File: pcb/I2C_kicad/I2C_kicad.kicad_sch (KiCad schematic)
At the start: 0 parts

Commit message: Reorganized file layout; created umbrella I2C folder for Kicad
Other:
- company: RoboCup -> (none)
- title: IMU -> (none)
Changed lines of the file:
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@@
 	(generator_version "10.0")
 	(paper "A4")
-	(title_block
-		(title "IMU")
-		(company "RoboCup")
-		(comment 1 "RoboCup DoubleKrish")
-	)
 	(sheet_instances
 		(path "/"

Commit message: added subsheets to the I2C file
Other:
- added sheet Color Sensor (ColorSensor.kicad_sch)
- added sheet GPIO expander (GPIOexpander.kicad_sch)
- added sheet Hall Effect Sensor (HallEffect.kicad_sch)
- added sheet IMU (IMU.kicad_sch)
- added sheet LED PWM Controller (LEDPWMController.kicad_sch)
- added sheet Temperature Sensor (TemperatureSensor.kicad_sch)
- company: (none) -> RoboCup
- title: (none) -> All 6 I2C Devices

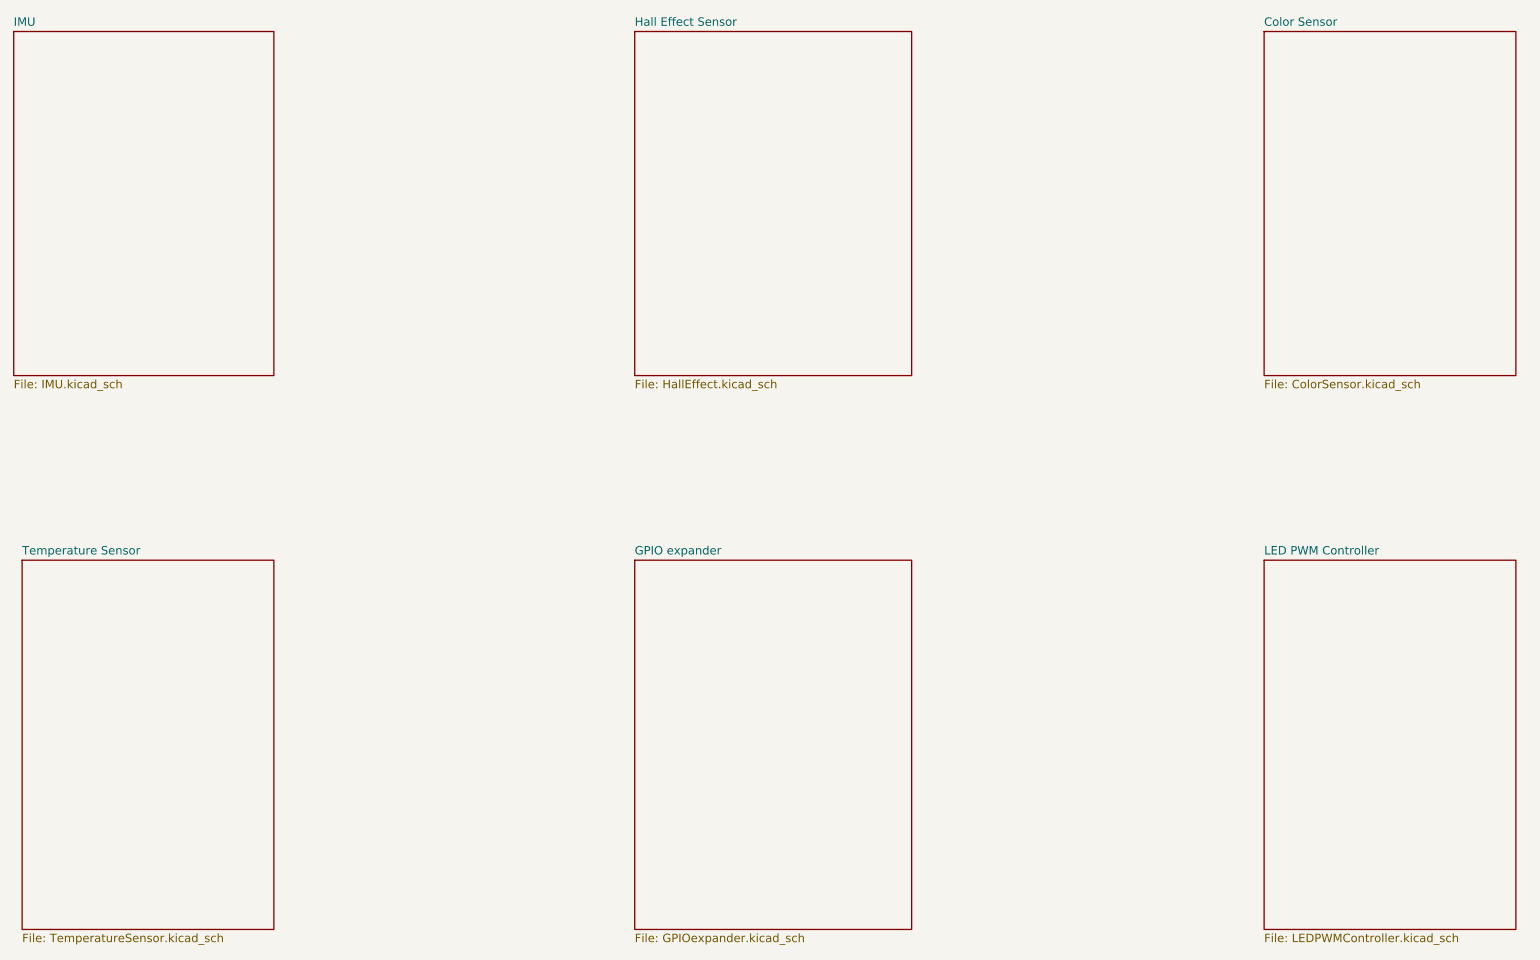
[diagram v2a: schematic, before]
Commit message: I worked on the color sensor and also the gpio expander. I added the pull ups for the SDA and SCL on the color sensor so no need to add any more. Just put do not populate for the other I2c devices
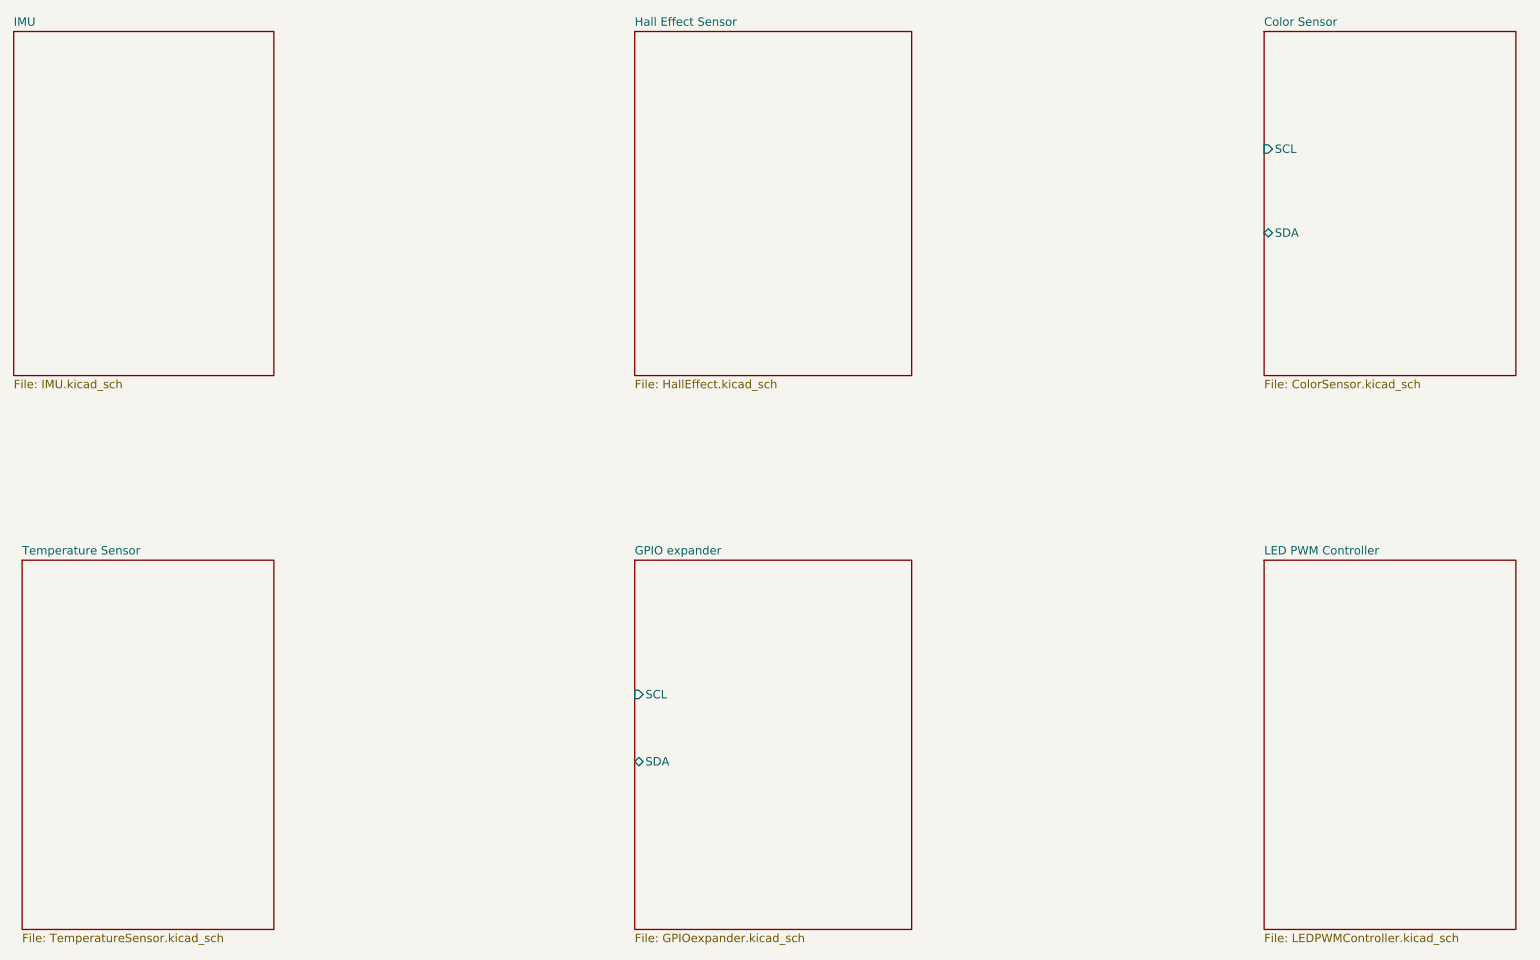
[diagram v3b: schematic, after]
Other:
- sheet Color Sensor ports: added SCL, SDA; removed none
- sheet GPIO expander ports: added SCL, SDA; removed none
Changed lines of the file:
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@@
+			)
+		)
+		(pin "SCL" input
+			(at 113.03 120.65 180)
+			(effects
+				(font
+					(size 1.27 1.27)
+				)
+				(justify left)
+			)
+		)
+		(pin "SDA" bidirectional
+			(at 113.03 130.81 180)
+			(effects
+				(font
+					(size 1.27 1.27)
+				)
+				(justify left)
 			)
 		)
@@
 			)
 		)
+		(pin "SCL" input
+			(at 208.28 38.1 180)
+			(effects
+				(font
+					(size 1.27 1.27)
+				)
+				(justify left)
+			)
+		)
+		(pin "SDA" bidirectional
+			(at 208.28 50.8 180)
+			(effects
+				(font
+					(size 1.27 1.27)
+				)
+				(justify left)
+			)
+		)

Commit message: Add IMU, Hall effect, and temp sensor sheets
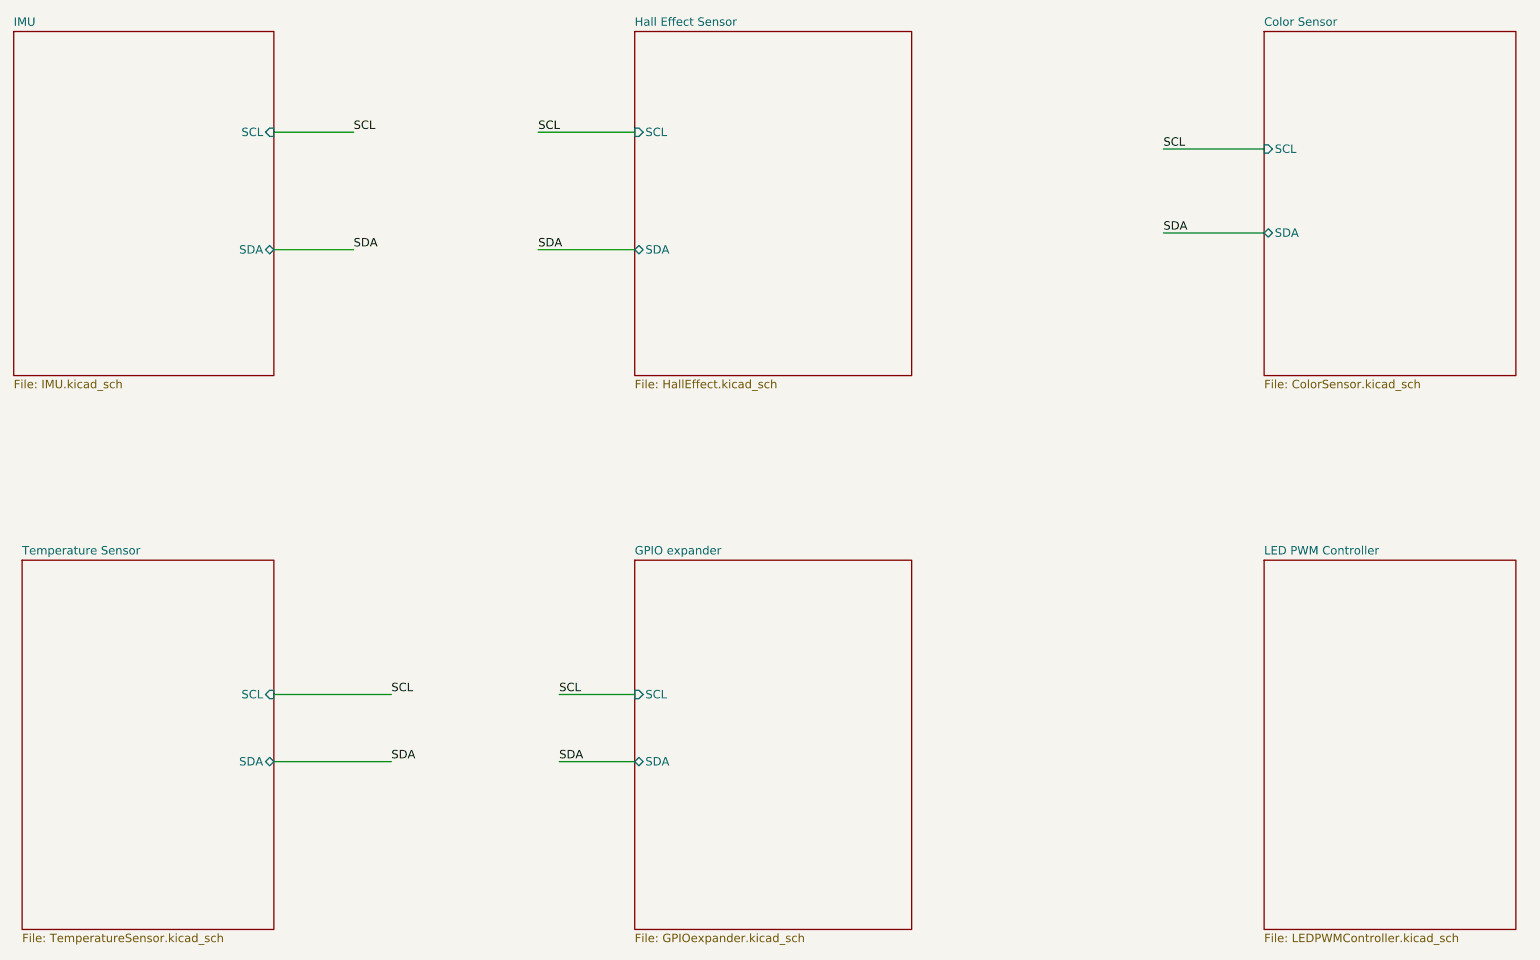
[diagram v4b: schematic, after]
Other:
- sheet Hall Effect Sensor ports: added SCL, SDA; removed none
- sheet IMU ports: added SCL, SDA; removed none
- sheet Temperature Sensor ports: added SCL, SDA; removed none
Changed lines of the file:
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@@
 		(comment 1 "Sean Hall")
+	)
+	(wire
+		(pts
+			(xy 98.425 53.34) (xy 113.03 53.34)
+		)
+		(stroke
+			(width 0)
+			(type default)
+		)
+	)
+	(wire
+		(pts
+			(xy 58.42 35.56) (xy 70.485 35.56)
+		)
+		(stroke
+			(width 0)
+			(type default)
+		)
+	)
+	(wire
+		(pts
+			(xy 193.04 38.1) (xy 208.28 38.1)
+		)
+		(stroke
+			(width 0)
+			(type default)
+		)
+	)
+	(wire
+		(pts
+			(xy 58.42 53.34) (xy 70.485 53.34)
+		)
+		(stroke
+			(width 0)
+			(type default)
+		)
+	)
+	(wire
+		(pts
+			(xy 58.42 130.81) (xy 76.2 130.81)
+		)
+		(stroke
+			(width 0)
+			(type default)
+		)
+	)
+	(wire
+		(pts
+			(xy 98.425 35.56) (xy 113.03 35.56)
+		)
+		(stroke
+			(width 0)
+			(type default)
+		)
+	)
+	(wire
+		(pts
+			(xy 101.6 130.81) (xy 113.03 130.81)
+		)
+		(stroke
+			(width 0)
+			(type default)
+		)
+	)
+	(wire
+		(pts
+			(xy 101.6 120.65) (xy 113.03 120.65)
+		)
+		(stroke
+			(width 0)
+			(type default)
+		)
+	)
+	(wire
+		(pts
+			(xy 193.04 50.8) (xy 208.28 50.8)
+		)
+		(stroke
+			(width 0)
+			(type default)
+		)
+	)
+	(wire
+		(pts
+			(xy 58.42 120.65) (xy 76.2 120.65)
+		)
+		(stroke
+			(width 0)
+			(type default)
+		)
+	)
+	(label "SDA"
+		(at 70.485 53.34 0)
+		(effects
+			(font
+				(size 1.27 1.27)
+			)
+			(justify left bottom)
+		)
+	)
+	(label "SCL"
+		(at 101.6 120.65 0)
+		(effects
+			(font
+				(size 1.27 1.27)
+			)
+			(justify left bottom)
+		)
+	)
+	(label "SCL"
+		(at 193.04 38.1 0)
+		(effects
+			(font
+				(size 1.27 1.27)
+			)
+			(justify left bottom)
+		)
+	)
+	(label "SDA"
+		(at 76.2 130.81 0)
+		(effects
+			(font
+				(size 1.27 1.27)
+			)
+			(justify left bottom)
+		)
+	)
+	(label "SCL"
+		(at 98.425 35.56 0)
+		(effects
+			(font
+				(size 1.27 1.27)
+			)
+			(justify left bottom)
+		)
+	)
+	(label "SDA"
+		(at 101.6 130.81 0)
+		(effects
+			(font
+				(size 1.27 1.27)
+			)
+			(justify left bottom)
+		)
+	)
+	(label "SDA"
+		(at 193.04 50.8 0)
+		(effects
+			(font
+				(size 1.27 1.27)
+			)
+			(justify left bottom)
+		)
+	)
+	(label "SDA"
+		(at 98.425 53.34 0)
+		(effects
+			(font
+				(size 1.27 1.27)
+			)
+			(justify left bottom)
+		)
+	)
+	(label "SCL"
+		(at 70.485 35.56 0)
+		(effects
+			(font
+				(size 1.27 1.27)
+			)
+			(justify left bottom)
+		)
+	)
+	(label "SCL"
+		(at 76.2 120.65 0)
+		(effects
+			(font
+				(size 1.27 1.27)
+			)
+			(justify left bottom)
+		)
 	)
 	(sheet
@@
 			)
 		)
+		(pin "SCL" input
+			(at 58.42 35.56 0)
+			(effects
+				(font
+					(size 1.27 1.27)
+				)
+				(justify right)
+			)
+		)
+		(pin "SDA" bidirectional
+			(at 58.42 53.34 0)
+			(effects
+				(font
+					(size 1.27 1.27)
+				)
+				(justify right)
+			)
+		)
 		(instances
 			(project "I2C_kicad"
@@
 			)
 		)
+		(pin "SCL" input
+			(at 58.42 120.65 0)
+			(effects
+				(font
+					(size 1.27 1.27)
+				)
+				(justify right)
+			)
+		)
+		(pin "SDA" bidirectional
+			(at 58.42 130.81 0)
+			(effects
+				(font
+					(size 1.27 1.27)
+				)
+				(justify right)
+			)
+		)
 		(instances
 			(project "I2C_kicad"
@@
 			)
 		)
+		(pin "SCL" input
+			(at 113.03 35.56 180)
+			(effects
+				(font
+					(size 1.27 1.27)
+				)
+				(justify left)
+			)
+		)
+		(pin "SDA" bidirectional
+			(at 113.03 53.34 180)
+			(effects
+				(font
+					(size 1.27 1.27)
+				)
+				(justify left)
+			)
+		)

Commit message: work was done
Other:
- sheet LED PWM Controller ports: added SCL, SDA; removed none
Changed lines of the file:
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@@
+	(wire
+		(pts
+			(xy 190.5 120.65) (xy 208.28 120.65)
+		)
+		(stroke
+			(width 0)
+			(type default)
+		)
+	)
 	(wire
 		(pts
@@
 		(pts
 			(xy 58.42 130.81) (xy 76.2 130.81)
+		)
+		(stroke
+			(width 0)
+			(type default)
+		)
+	)
+	(wire
+		(pts
+			(xy 190.5 130.81) (xy 208.28 130.81)
 		)
 		(stroke
@@
 		)
 	)
+	(label "SDA"
+		(at 190.5 130.81 0)
+		(effects
+			(font
+				(size 1.27 1.27)
+			)
+			(justify left bottom)
+		)
+	)
 	(label "SCL"
 		(at 101.6 120.65 0)
@@
 	(label "SDA"
 		(at 76.2 130.81 0)
+		(effects
+			(font
+				(size 1.27 1.27)
+			)
+			(justify left bottom)
+		)
+	)
+	(label "SCL"
+		(at 190.5 120.65 0)
 		(effects
 			(font
@@
 			)
 		)
+		(pin "SCL" input
+			(at 208.28 120.65 180)
+			(effects
+				(font
+					(size 1.27 1.27)
+				)
+				(justify left)
+			)
+		)
+		(pin "SDA" bidirectional
+			(at 208.28 130.81 180)
+			(effects
+				(font
+					(size 1.27 1.27)
+				)
+				(justify left)
+			)
+		)
